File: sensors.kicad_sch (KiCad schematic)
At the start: 18 parts, among them IC2 MMC5603NJ, IC3 ICM-42670-P, IC4 MAX-F10S-00B, IC5 ICM-45686, U2 BMP581

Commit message: pcb coming along, schematic way more done - I now have a lot more respect for hardware people than I did earlier
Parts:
- removed AE1: Antenna, symbol Device:Antenna
- added J1: antenna, Connector_Coaxial:U.FL_Molex_MCRF_73412-0110_Vertical, symbol Connector:Conn_Coaxial_Small
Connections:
- net GND: now also J1.2 (Ext)
- net at IC4.11 (RF_IN): now also J1.1 (In)
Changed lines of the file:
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@@
 	)
 	(junction
+		(at 198.12 53.34)
+		(diameter 0)
+		(color 0 0 0 0)
+	)
+	(junction
 		(at 143.51 113.03)
 		(diameter 0)
@@
 	(wire
 		(pts
+			(xy 191.77 53.34) (xy 198.12 53.34)
+		)
+		(stroke
+			(width 0)
+			(type default)
+		)
+	)
+	(wire
+		(pts
 			(xy 52.07 143.51) (xy 52.07 142.24)
 		)
@@
 	(wire
 		(pts
+			(xy 191.77 50.8) (xy 191.77 53.34)
+		)
+		(stroke
+			(width 0)
+			(type default)
+		)
+	)
+	(wire
+		(pts
 			(xy 34.29 143.51) (xy 34.29 161.29)
 		)
@@
 	)
 	(symbol
-		(lib_id "Device:Antenna")
-		(at 196.85 45.72 0)
-		(unit 1)
-		(exclude_from_sim no)
-		(in_bom yes)
-		(on_board yes)
-		(dnp no)
-		(property "Reference" "AE1"
-			(at 198.12 39.624 0)
-			(effects
-				(font
-					(size 1.27 1.27)
-				)
-				(justify left)
-			)
-		)
-		(property "Value" "Antenna"
-			(at 199.898 41.402 0)
-			(effects
-				(font
-					(size 1.27 1.27)
-				)
-				(justify left)
-			)
-		)
-		(property "Footprint" ""
-			(at 196.85 45.72 0)
-			(effects
-				(font
-					(size 1.27 1.27)
-				)
-				(hide yes)
-			)
-		)
-		(property "Datasheet" "~"
-			(at 196.85 45.72 0)
-			(effects
-				(font
-					(size 1.27 1.27)
-				)
-				(hide yes)
-			)
-		)
-		(property "Description" "Antenna"
-			(at 196.85 45.72 0)
-			(effects
-				(font
-					(size 1.27 1.27)
-				)
-				(hide yes)
-			)
-		)
-		(pin "1"
-		)
-		(instances
-			(project ""
-				(path "/d0cafa98-cc2a-4ab3-8dbc-f937bedf434b/3f7351fc-adab-43cb-953e-682e25e079d7"
-					(reference "AE1")
-					(unit 1)
-				)
-			)
-		)
-	)
-	(symbol
 		(lib_id "power:GND")
 		(at 49.53 185.42 0)
@@
 					(unit 1)
 				)
+			)
+		)
+	)
+	(symbol
+		(lib_id "Connector:Conn_Coaxial_Small")
+		(at 194.31 50.8 180)
+		(unit 1)
+		(exclude_from_sim no)
+		(in_bom yes)
+		(on_board yes)
+		(dnp no)
+		(fields_autoplaced yes)
+		(property "Reference" "J1"
+			(at 194.8295 44.45 0)
+			(effects
+				(font
+					(size 1.27 1.27)
+				)
+			)
+		)
+		(property "Value" "antenna"
+			(at 194.8295 46.99 0)
+			(effects
+				(font
+					(size 1.27 1.27)
+				)
+			)
+		)
+		(property "Footprint" "Connector_Coaxial:U.FL_Molex_MCRF_73412-0110_Vertical"
+			(at 194.31 50.8 0)
+			(effects
+				(font
+					(size 1.27 1.27)
+				)
+				(hide yes)
+			)
+		)
+		(property "Datasheet" "~"
+			(at 194.31 50.8 0)
+			(effects
+				(font
+					(size 1.27 1.27)
+				)
+				(hide yes)
+			)
+		)
+		(property "Description" "small coaxial connector (BNC, SMA, SMB, SMC, Cinch/RCA, LEMO, ...)"
+			(at 194.31 50.8 0)
+			(effects
+				(font
+					(size 1.27 1.27)
+				)
+				(hide yes)
+			)
+		)
+		(pin "1"
+		)
+		(pin "2"
+		)
+		(instances
+			(project ""
+				(path "/d0cafa98-cc2a-4ab3-8dbc-f937bedf434b/3f7351fc-adab-43cb-953e-682e25e079d7"
+					(reference "J1")
+					(unit 1)
+				)

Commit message: tons of work, see journal for details
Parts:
- removed C17: 0.1uF, Capacitor_SMD:C_0402_1005Metric, symbol Device:C
- removed C18: 10uF, Capacitor_SMD:C_0603_1608Metric, symbol Device:C
- removed C20, C24: 2.2uF, Capacitor_SMD:C_0603_1608Metric, symbol Device:C
- removed IC2: MMC5603NJ, footprints:MMC5603NJ, symbol MMC5603NJ:MMC5603NJ
- removed IC4: MAX-F10S-00B, footprints:MAXF10S00B, symbol MAX-F10S-00B:MAX-F10S-00B
- removed J1: antenna, Connector_Coaxial:U.FL_Molex_MCRF_73412-0110_Vertical, symbol Connector:Conn_Coaxial_Small
- removed R6, R7: 2.7k, Resistor_SMD:R_0402_1005Metric, symbol Device:R
- added IC2: MMC5983MA, MMC5983MA, symbol MMC5983MA:MMC5983MA
- C16: value 2.2uF -> 10uF; footprint Capacitor_SMD:C_0603_1608Metric -> (none)
- C22, C23: value 10nF -> 0.1uF
- IC3: value ICM-42670-P -> ICM-45686
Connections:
- net +3.3V: now also IC2.13 (VDDIO), IC2.2 (VDD), IC2.4 (SPI_CS); no longer C16.2, IC3.1 (AP_SDO_/_AP_AD0)
- net GND: now also C16.2, IC3.1 (AP_SDO_/_AP_AD0), IC2.11 (GND_2), IC2.9 (GND_1); no longer C16.1
- net i2c1_sck: now also IC2.1 (SCL/SPI_SCK)
- net i2c1_sda: now also IC2.16 (SDA/SPI_SDI)
- net highrate_highg_int1 renamed imu1_int1
- net highrate_highg_int2 renamed imu1_int2
- net lowrate_lowg_int1 renamed imu2_int1
- net lowrate_lowg_int2 renamed imu2_int2
- new net: C16.1, IC2.10 (CAP)
- new net mag_int: IC2.15 (INT)
- no-connect marks 13 -> 15
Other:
- moved on the sheet: C21, C22, C25, IC3

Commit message: tons of progress on schematic and pcb - see journal for details
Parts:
- C24: renamed from C16; footprint (none) -> Capacitor_SMD:C_0603_1608Metric
- IC5: renamed from IC2; footprint MMC5983MA -> footprints:MMC5983MA
- renumbered C15 to C19, C23 to C20, C25 to C21, C21 to C23, IC5 to IC3, IC3 to IC4, U2 to U3
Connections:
- net imu1_int2: no longer names the net of IC3.9 (INT2)
- net imu2_int2: no longer names the net of IC4.9 (INT2)
- no-connect marks 15 -> 17

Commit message: worked mainly on pcb
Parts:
- C20, C21, C22, C23: value 0.1uF -> 100nF
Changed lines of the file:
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@@
 			)
 		)
-		(property "Value" "0.1uF"
+		(property "Value" "100nF"
 			(at 33.528 116.586 0)
 			(effects
@@
 			)
 		)
-		(property "Value" "0.1uF"
+		(property "Value" "100nF"
 			(at 152.654 101.6 0)
 			(effects
@@
 			)
 		)
-		(property "Value" "0.1uF"
+		(property "Value" "100nF"
 			(at 80.01 101.5999 0)
 			(effects
@@
 			)
 		)
-		(property "Value" "0.1uF"
+		(property "Value" "100nF"
 			(at 107.188 116.586 0)
 			(effects

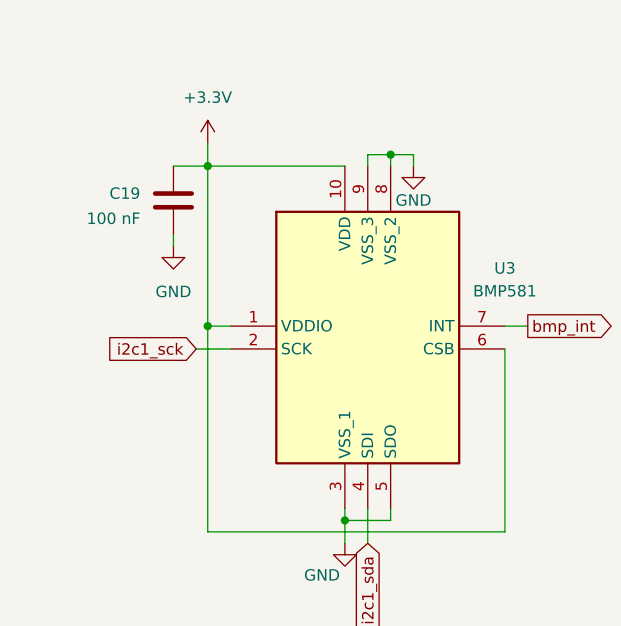
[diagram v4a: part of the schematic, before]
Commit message: basically just decoupling capacitors that I forgot
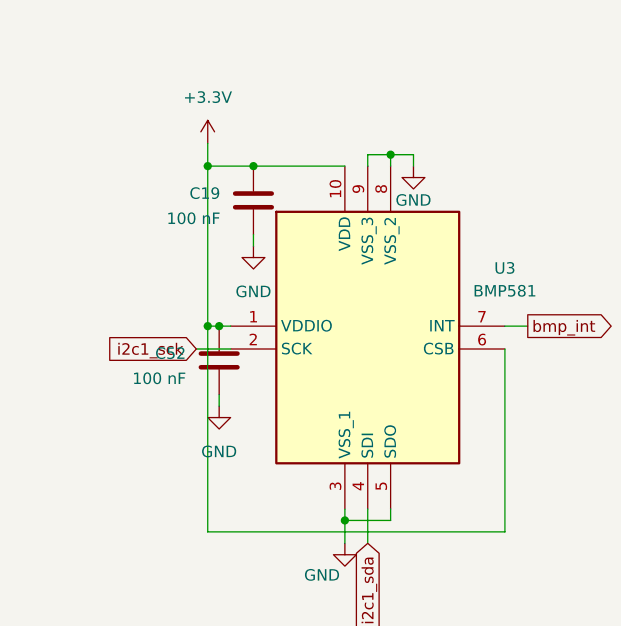
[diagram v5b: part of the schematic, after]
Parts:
- added C52: 100 nF, Capacitor_SMD:C_0402_1005Metric, symbol Device:C
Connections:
- net +3.3V: now also C52.2
- net GND: now also C52.1
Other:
- moved on the sheet: C19
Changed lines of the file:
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@@
+	)
+	(junction
+		(at 39.37 143.51)
+		(diameter 0)
+		(color 0 0 0 0)
 	)
 	(junction
@@
 		(color 0 0 0 0)
 	)
+	(junction
+		(at 35.56 161.29)
+		(diameter 0)
+		(color 0 0 0 0)
+	)
 	(no_connect
 		(at 148.59 83.82)
@@
 	(wire
 		(pts
-			(xy 30.48 151.13) (xy 30.48 152.4)
-		)
-		(stroke
-			(width 0)
-			(type default)
-		)
-	)
-	(wire
-		(pts
 			(xy 34.29 184.15) (xy 67.31 184.15)
 		)
@@
 	(wire
 		(pts
+			(xy 35.56 168.91) (xy 35.56 170.18)
+		)
+		(stroke
+			(width 0)
+			(type default)
+		)
+	)
+	(wire
+		(pts
 			(xy 123.19 109.22) (xy 123.19 110.49)
 		)
@@
 	(wire
 		(pts
-			(xy 34.29 161.29) (xy 36.83 161.29)
+			(xy 34.29 161.29) (xy 35.56 161.29)
 		)
 		(stroke
@@
 	(wire
 		(pts
+			(xy 39.37 143.51) (xy 49.53 143.51)
+		)
+		(stroke
+			(width 0)
+			(type default)
+		)
+	)
+	(wire
+		(pts
 			(xy 34.29 143.51) (xy 34.29 161.29)
 		)
@@
 	(wire
 		(pts
-			(xy 34.29 143.51) (xy 49.53 143.51)
+			(xy 34.29 143.51) (xy 39.37 143.51)
 		)
 		(stroke
@@
 	(wire
 		(pts
-			(xy 30.48 143.51) (xy 34.29 143.51)
-		)
-		(stroke
-			(width 0)
-			(type default)
-		)
-	)
-	(wire
-		(pts
 			(xy 27.94 91.44) (xy 29.21 91.44)
+		)
+		(stroke
+			(width 0)
+			(type default)
+		)
+	)
+	(wire
+		(pts
+			(xy 35.56 161.29) (xy 36.83 161.29)
+		)
+		(stroke
+			(width 0)
+			(type default)
+		)
+	)
+	(wire
+		(pts
+			(xy 39.37 151.13) (xy 39.37 152.4)
 		)
 		(stroke
@@
 	(symbol
 		(lib_id "power:GND")
+		(at 35.56 170.18 0)
+		(unit 1)
+		(exclude_from_sim no)
+		(in_bom yes)
+		(on_board yes)
+		(dnp no)
+		(fields_autoplaced yes)
+		(property "Reference" "#PWR097"
+			(at 35.56 176.53 0)
+			(effects
+				(font
+					(size 1.27 1.27)
+				)
+				(hide yes)
+			)
+		)
+		(property "Value" "GND"
+			(at 35.56 175.26 0)
+			(effects
+				(font
+					(size 1.27 1.27)
+				)
+			)
+		)
+		(property "Footprint" ""
+			(at 35.56 170.18 0)
+			(effects
+				(font
+					(size 1.27 1.27)
+				)
+				(hide yes)
+			)
+		)
+		(property "Datasheet" ""
+			(at 35.56 170.18 0)
+			(effects
+				(font
+					(size 1.27 1.27)
+				)
+				(hide yes)
+			)
+		)
+		(property "Description" "Power symbol creates a global label with name \"GND\" , ground"
+			(at 35.56 170.18 0)
+			(effects
+				(font
+					(size 1.27 1.27)
+				)
+				(hide yes)
+			)
+		)
+		(pin "1"
+		)
+		(instances
+			(project "stDevboard"
+				(path "/d0cafa98-cc2a-4ab3-8dbc-f937bedf434b/3f7351fc-adab-43cb-953e-682e25e079d7"
+					(reference "#PWR097")
+					(unit 1)
+				)
+			)
+		)
+	)
+	(symbol
+		(lib_id "power:GND")
 		(at 57.15 143.51 0)
 		(unit 1)
@@
 	)
 	(symbol
+		(lib_id "Device:C")
+		(at 35.56 165.1 180)
+		(unit 1)
+		(exclude_from_sim no)
+		(in_bom yes)
+		(on_board yes)
+		(dnp no)
+		(property "Reference" "C52"
+			(at 28.448 164.338 0)
+			(effects
+				(font
+					(size 1.27 1.27)
+				)
+				(justify right)
+			)
+		)
+		(property "Value" "100 nF"
+			(at 25.908 167.132 0)
+			(effects
+				(font
+					(size 1.27 1.27)
+				)
+				(justify right)
+			)
+		)
+		(property "Footprint" "Capacitor_SMD:C_0402_1005Metric"
+			(at 34.5948 161.29 0)
+			(effects
+				(font
+					(size 1.27 1.27)
+				)
+				(hide yes)
+			)
+		)
+		(property "Datasheet" "~"
+			(at 35.56 165.1 0)
+			(effects
+				(font
+					(size 1.27 1.27)
+				)
+				(hide yes)
+			)
+		)
+		(property "Description" "Unpolarized capacitor"
+			(at 35.56 165.1 0)
+			(effects
+				(font
+					(size 1.27 1.27)
+				)
+				(hide yes)
+			)
+		)
+		(pin "1"
+		)
+		(pin "2"
+		)
+		(instances
+			(project "stDevboard"
+				(path "/d0cafa98-cc2a-4ab3-8dbc-f937bedf434b/3f7351fc-adab-43cb-953e-682e25e079d7"
+					(reference "C52")
+					(unit 1)
+				)
+			)
+		)
+	)
+	(symbol
 		(lib_id "MMC5983MA:MMC5983MA")
 		(at 189.23 78.74 0)
@@
 	(symbol
 		(lib_id "Device:C")
-		(at 30.48 147.32 180)
+		(at 39.37 147.32 180)
 		(unit 1)
 		(exclude_from_sim no)
@@
 		(dnp no)
 		(property "Reference" "C19"
-			(at 23.368 146.558 0)
+			(at 32.258 146.558 0)
 			(effects
 				(font
@@
 		)
 		(property "Value" "100 nF"
-			(at 20.828 149.352 0)
+			(at 29.718 149.352 0)
 			(effects
 				(font
@@
 		)
 		(property "Footprint" "Capacitor_SMD:C_0402_1005Metric"
-			(at 29.5148 143.51 0)
+			(at 38.4048 143.51 0)
 			(effects
 				(font
@@
 		)
 		(property "Datasheet" "~"
-			(at 30.48 147.32 0)
+			(at 39.37 147.32 0)
 			(effects
 				(font
@@
 		)
 		(property "Description" "Unpolarized capacitor"
-			(at 30.48 147.32 0)
+			(at 39.37 147.32 0)
 			(effects
 				(font
@@
 	(symbol
 		(lib_id "power:GND")
-		(at 30.48 152.4 0)
+		(at 39.37 152.4 0)
 		(unit 1)
 		(exclude_from_sim no)
@@
 		(fields_autoplaced yes)
 		(property "Reference" "#PWR047"
-			(at 30.48 158.75 0)
+			(at 39.37 158.75 0)
 			(effects
 				(font
@@
 		)
 		(property "Value" "GND"
-			(at 30.48 157.48 0)
+			(at 39.37 157.48 0)
 			(effects
 				(font
@@
 		)
 		(property "Footprint" ""
-			(at 30.48 152.4 0)
+			(at 39.37 152.4 0)
 			(effects
 				(font
@@
 		)
 		(property "Datasheet" ""
-			(at 30.48 152.4 0)
+			(at 39.37 152.4 0)
 			(effects
 				(font
@@
 		)
 		(property "Description" "Power symbol creates a global label with name \"GND\" , ground"
-			(at 30.48 152.4 0)
-			(effects
-				(font
+			(at 39.37 152.4 0)
+			(effects
+				(font

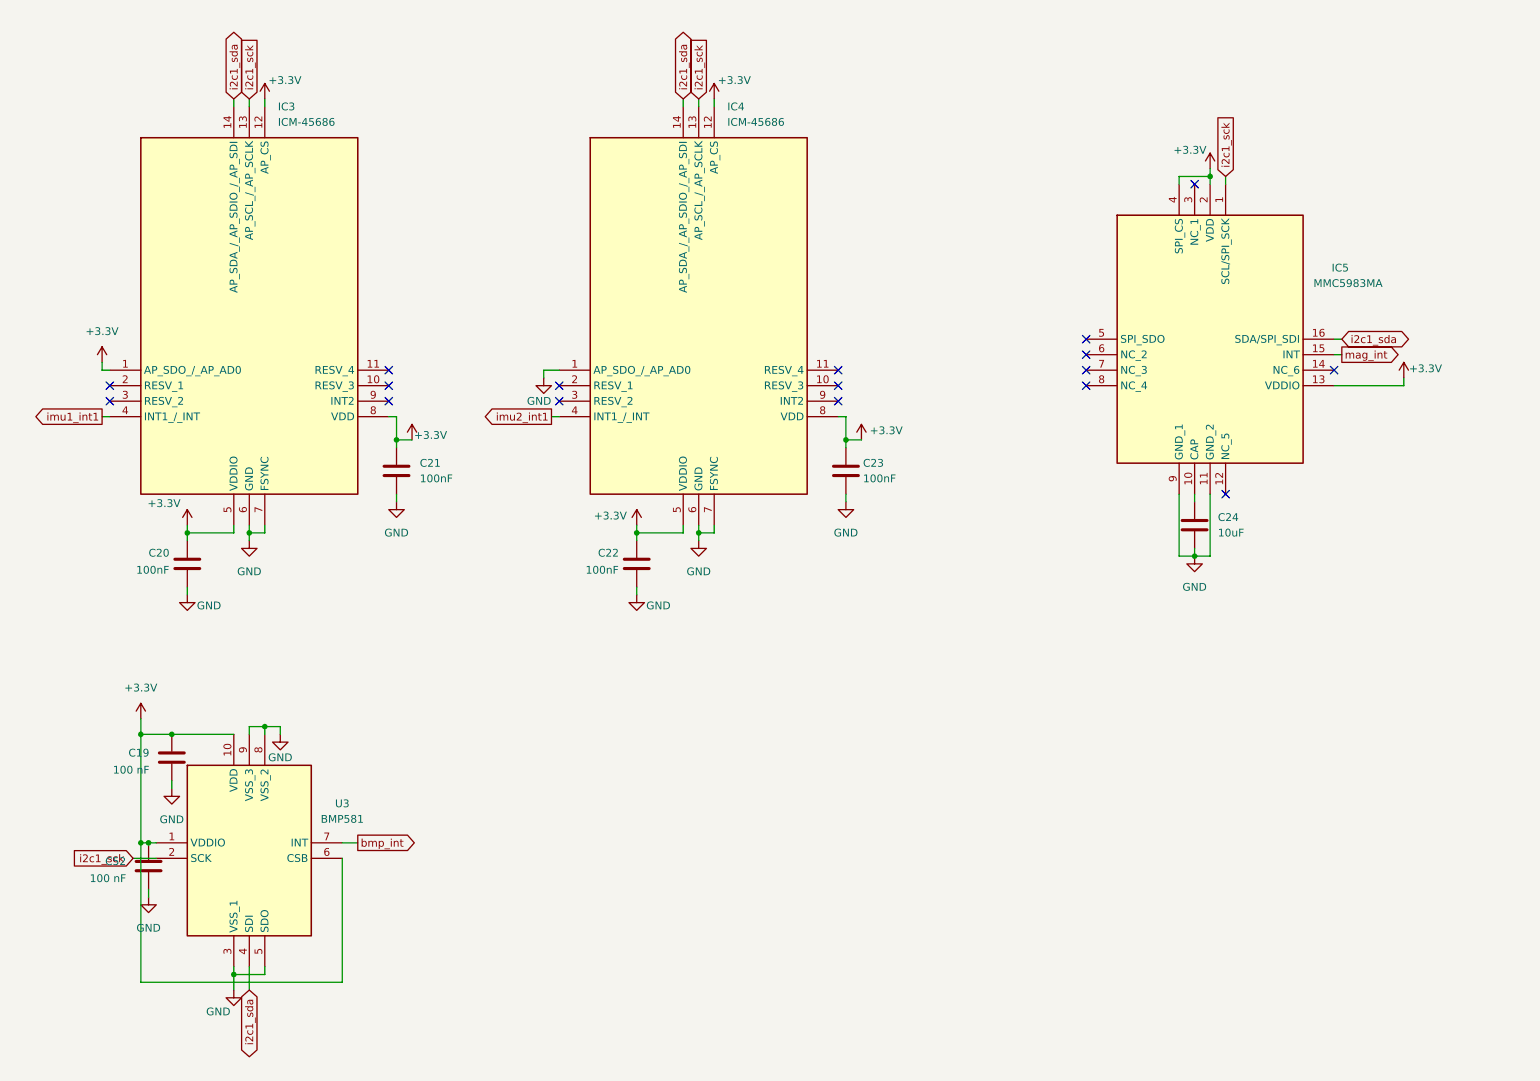
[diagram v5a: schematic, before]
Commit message: added decoupling caps, added high g accel - about to redo basically all of the pin allocations on the mpu so I can have a high speed and low speed i2c
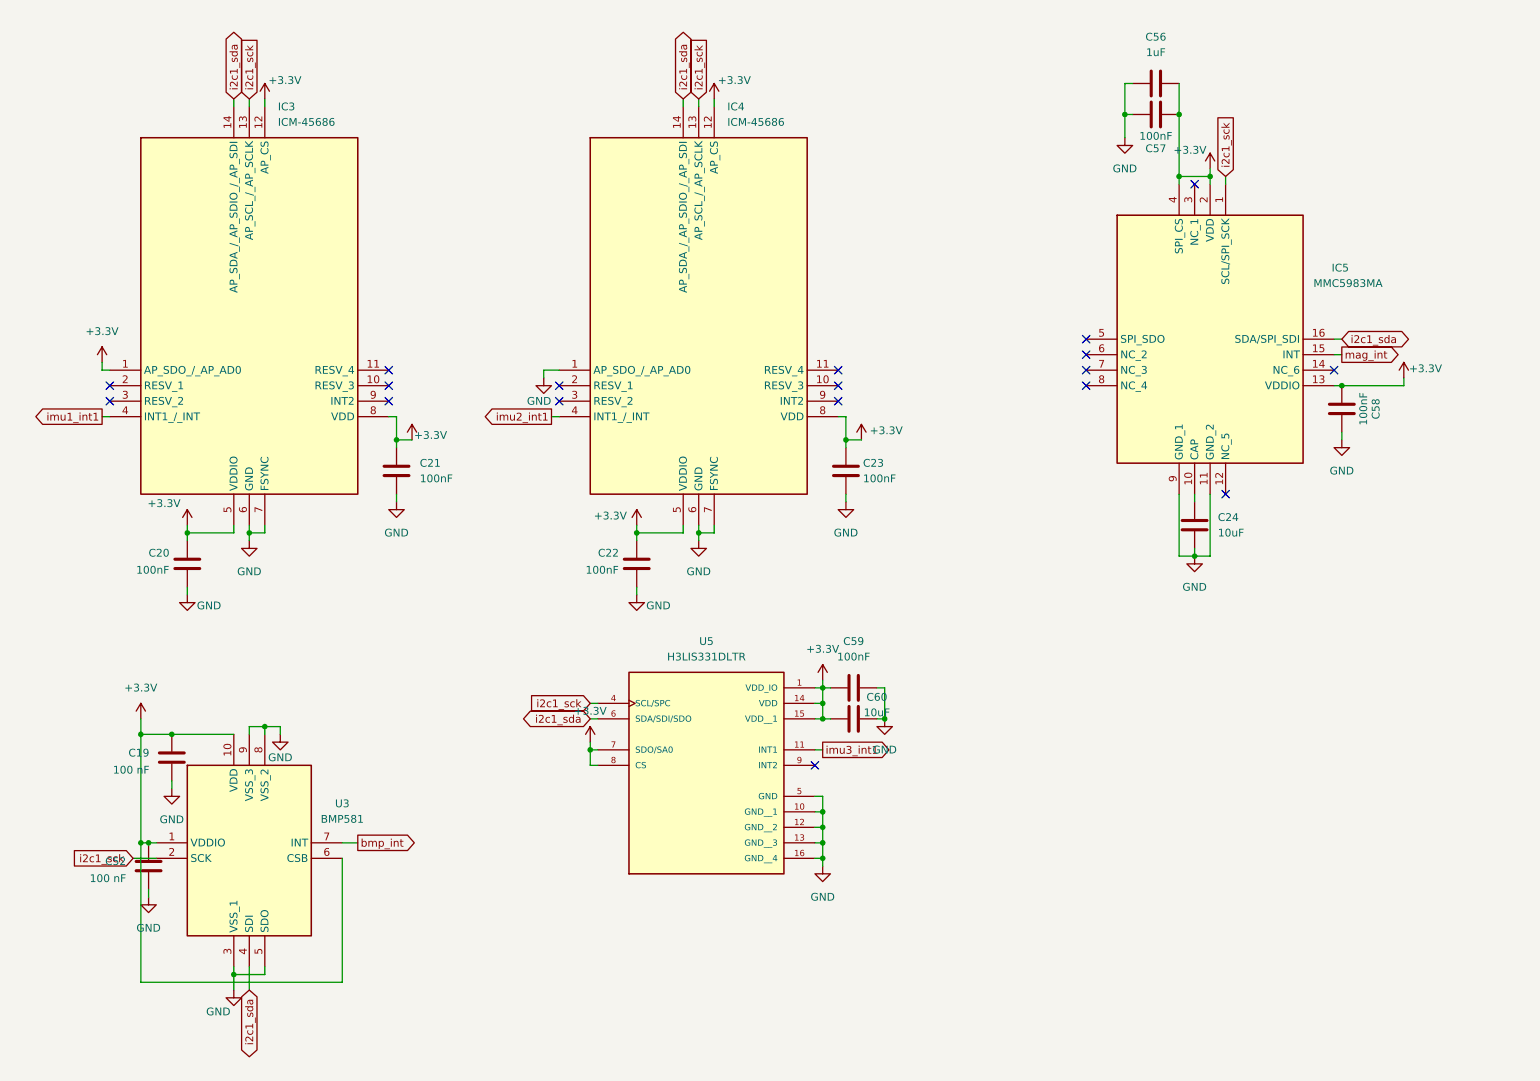
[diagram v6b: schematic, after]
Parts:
- added C56: 1uF, symbol Device:C
- added C57, C58, C59: 100nF, symbol Device:C
- added C60: 10uF, symbol Device:C
- added U5: H3LIS331DLTR, H3LIS331DLTR:QFN300X300X100-16N, symbol H3LIS331DLTR:H3LIS331DLTR
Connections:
- net +3.3V: now also C56.2, C57.2, C58.2, C59.1, C60.1, U5.1 (VDD_IO), U5.14 (VDD), U5.15 (VDD__1), U5.7 (SDO/SA0), U5.8 (CS)
- net GND: now also C56.1, C57.1, C58.1, C59.2, C60.2, U5.10 (GND__1), U5.12 (GND__2), U5.13 (GND__3), U5.16 (GND__4), U5.5 (GND)
- net i2c1_sck: now also U5.4 (SCL/SPC)
- net i2c1_sda: now also U5.6 (SDA/SDI/SDO)
- new net imu3_int1: U5.11 (INT1)
- no-connect marks 17 -> 18
